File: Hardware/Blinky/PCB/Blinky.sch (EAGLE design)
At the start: 29 parts, among them Q1 IRLML2502, Q2 IRLML2502, Q3 IRLML2502, U1 ATMEGAU2-AU, U2 MTCH101, U3 TS3USB30EDGSR, X1 USB-A-PCB, X2 USB-A-PCB, Y1 ABM3

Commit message: Most of the PCB layout is done.
Still missing is the touch sensor disguised as logo (hello issue #10).
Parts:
- removed C6: 100n, rcl:C-EUC0805
- added U$1: BISS-LOGO, mibe:BISS-LOGO
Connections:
- net N$1 renamed D+_MIC
- net N$12 renamed D2-
- net N$13 renamed D2+
- net N$14 renamed D1-
- net N$15 renamed D1+
- net N$2 renamed D-_MIC
- net N$20 renamed RESET
- net N$21 renamed GND_LED_R
- net N$22 renamed GND_LED_G
- net N$23 renamed GND_LED_B
- net N$3 renamed UCAP
- net N$4 renamed TOUCH
- net N$7 renamed D+_CON
- net N$8 renamed D-_CON
- net ULEDB renamed V_LED_B
- net ULEDG renamed V_LED_G
- net ULEDR renamed V_LED_R
- new net TOUCH_PAD: U$1.P$1, U2.MTI
- net GND: now also U1.PD5; no longer C6.2
- net LED_G: now also U1.PC7
- net VCC: no longer C6.1
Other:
- moved on the sheet: C2, C3, Y1
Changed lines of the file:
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@@
 <part name="C4" library="rcl" deviceset="C-EU" device="C0805" value="100n"/>
 <part name="C5" library="rcl" deviceset="C-EU" device="C0805" value="100n"/>
-<part name="C6" library="rcl" deviceset="C-EU" device="C0805" value="100n"/>
 <part name="P+3" library="supply1" deviceset="VCC" device=""/>
 <part name="GND6" library="supply1" deviceset="GND" device=""/>
@@
 <part name="R10" library="rcl" deviceset="R-EU_" device="R0805" value="64.9"/>
 <part name="R11" library="rcl" deviceset="R-EU_" device="R0805" value="64.9"/>
+<part name="U$1" library="mibe" deviceset="BISS-LOGO" device=""/>
+<part name="GND9" library="supply1" deviceset="GND" device=""/>
 </parts>
 <sheets>
@@
 <instance part="GND2" gate="1" x="200.66" y="144.78"/>
 <instance part="GND3" gate="1" x="73.66" y="99.06"/>
-<instance part="C2" gate="G$1" x="187.96" y="114.3" rot="R90"/>
-<instance part="C3" gate="G$1" x="187.96" y="109.22" smashed="yes" rot="R90">
-<attribute name="NAME" x="187.579" y="103.124" size="1.778" layer="95" rot="R90"/>
-<attribute name="VALUE" x="192.659" y="103.124" size="1.778" layer="96" rot="R90"/>
+<instance part="C2" gate="G$1" x="193.04" y="114.3" rot="R90"/>
+<instance part="C3" gate="G$1" x="193.04" y="109.22" smashed="yes" rot="R90">
+<attribute name="NAME" x="192.659" y="103.124" size="1.778" layer="95" rot="R90"/>
+<attribute name="VALUE" x="197.739" y="103.124" size="1.778" layer="96" rot="R90"/>
 </instance>
-<instance part="GND4" gate="1" x="200.66" y="104.14"/>
-<instance part="Y1" gate="G$1" x="180.34" y="111.76" rot="R90"/>
+<instance part="GND4" gate="1" x="205.74" y="104.14"/>
+<instance part="Y1" gate="G$1" x="185.42" y="111.76" rot="R90"/>
 <instance part="R1" gate="G$1" x="121.92" y="124.46" smashed="yes">
 <attribute name="NAME" x="118.11" y="126.238" size="1.778" layer="95"/>
@@
 <instance part="C4" gate="G$1" x="63.5" y="33.02"/>
 <instance part="C5" gate="G$1" x="76.2" y="33.02"/>
-<instance part="C6" gate="G$1" x="88.9" y="33.02"/>
 <instance part="P+3" gate="VCC" x="53.34" y="40.64"/>
 <instance part="GND6" gate="1" x="53.34" y="22.86"/>
@@
 <instance part="R10" gate="G$1" x="233.68" y="93.98" rot="R90"/>
 <instance part="R11" gate="G$1" x="238.76" y="101.6" rot="R90"/>
+<instance part="U$1" gate="G$1" x="238.76" y="172.72"/>
+<instance part="GND9" gate="1" x="132.08" y="129.54"/>
 </instances>
 <busses>
@@
 <segment>
 <pinref part="GND4" gate="1" pin="GND"/>
-<wire x1="200.66" y1="114.3" x2="200.66" y2="109.22" width="0.1524" layer="91"/>
+<wire x1="205.74" y1="114.3" x2="205.74" y2="109.22" width="0.1524" layer="91"/>
 <pinref part="C2" gate="G$1" pin="2"/>
-<wire x1="200.66" y1="109.22" x2="200.66" y2="106.68" width="0.1524" layer="91"/>
-<wire x1="193.04" y1="114.3" x2="200.66" y2="114.3" width="0.1524" layer="91"/>
+<wire x1="205.74" y1="109.22" x2="205.74" y2="106.68" width="0.1524" layer="91"/>
+<wire x1="198.12" y1="114.3" x2="205.74" y2="114.3" width="0.1524" layer="91"/>
 <pinref part="C3" gate="G$1" pin="2"/>
-<wire x1="193.04" y1="109.22" x2="200.66" y2="109.22" width="0.1524" layer="91"/>
-<junction x="200.66" y="109.22"/>
+<wire x1="198.12" y1="109.22" x2="205.74" y2="109.22" width="0.1524" layer="91"/>
+<junction x="205.74" y="109.22"/>
 </segment>
 <segment>
@@
 <pinref part="GND6" gate="1" pin="GND"/>
 <wire x1="63.5" y1="25.4" x2="53.34" y2="25.4" width="0.1524" layer="91"/>
-<pinref part="C6" gate="G$1" pin="2"/>
 <wire x1="63.5" y1="25.4" x2="76.2" y2="25.4" width="0.1524" layer="91"/>
-<wire x1="76.2" y1="25.4" x2="88.9" y2="25.4" width="0.1524" layer="91"/>
-<wire x1="88.9" y1="25.4" x2="88.9" y2="27.94" width="0.1524" layer="91"/>
 <junction x="63.5" y="25.4"/>
 <pinref part="C5" gate="G$1" pin="2"/>
 <wire x1="76.2" y1="27.94" x2="76.2" y2="25.4" width="0.1524" layer="91"/>
-<junction x="76.2" y="25.4"/>
 </segment>
 <segment>
@@
 <junction x="233.68" y="45.72"/>
 </segment>
-</net>
-<net name="N$3" class="0">
+<segment>
+<pinref part="U1" gate="G$1" pin="PD5"/>
+<pinref part="GND9" gate="1" pin="GND"/>
+<wire x1="139.7" y1="134.62" x2="132.08" y2="134.62" width="0.1524" layer="91"/>
+<wire x1="132.08" y1="134.62" x2="132.08" y2="132.08" width="0.1524" layer="91"/>
+</segment>
+</net>
+<net name="UCAP" class="0">
 <segment>
 <pinref part="C1" gate="G$1" pin="1"/>
@@
 <segment>
 <pinref part="U1" gate="G$1" pin="XTAL1"/>
-<wire x1="175.26" y1="114.3" x2="180.34" y2="114.3" width="0.1524" layer="91"/>
+<wire x1="175.26" y1="114.3" x2="185.42" y2="114.3" width="0.1524" layer="91"/>
 <pinref part="Y1" gate="G$1" pin="2"/>
 <pinref part="C2" gate="G$1" pin="1"/>
-<wire x1="180.34" y1="114.3" x2="185.42" y2="114.3" width="0.1524" layer="91"/>
-<junction x="180.34" y="114.3"/>
+<wire x1="185.42" y1="114.3" x2="190.5" y2="114.3" width="0.1524" layer="91"/>
+<junction x="185.42" y="114.3"/>
 </segment>
 </net>
@@
 <pinref part="U1" gate="G$1" pin="XTAL2"/>
 <pinref part="Y1" gate="G$1" pin="1"/>
-<wire x1="180.34" y1="109.22" x2="175.26" y2="109.22" width="0.1524" layer="91"/>
+<wire x1="185.42" y1="109.22" x2="175.26" y2="109.22" width="0.1524" layer="91"/>
 <pinref part="C3" gate="G$1" pin="1"/>
-<wire x1="180.34" y1="109.22" x2="185.42" y2="109.22" width="0.1524" layer="91"/>
-<junction x="180.34" y="109.22"/>
-</segment>
-</net>
-<net name="N$1" class="0">
+<wire x1="185.42" y1="109.22" x2="190.5" y2="109.22" width="0.1524" layer="91"/>
+<junction x="185.42" y="109.22"/>
+</segment>
+</net>
+<net name="D+_MIC" class="0">
 <segment>
 <pinref part="R1" gate="G$1" pin="2"/>
@@
 </segment>
 </net>
-<net name="N$2" class="0">
+<net name="D-_MIC" class="0">
 <segment>
 <pinref part="U1" gate="G$1" pin="D-"/>
@@
 </segment>
 </net>
-<net name="N$7" class="0">
+<net name="D+_CON" class="0">
 <segment>
 <pinref part="R1" gate="G$1" pin="1"/>
@@
 </segment>
 </net>
-<net name="N$8" class="0">
+<net name="D-_CON" class="0">
 <segment>
 <pinref part="U3" gate="G$1" pin="D-"/>
@@
 <segment>
 <pinref part="U1" gate="G$1" pin="PC5"/>
-<wire x1="175.26" y1="124.46" x2="213.36" y2="124.46" width="0.1524" layer="91"/>
+<wire x1="175.26" y1="124.46" x2="180.34" y2="124.46" width="0.1524" layer="91"/>
+<wire x1="180.34" y1="124.46" x2="213.36" y2="124.46" width="0.1524" layer="91"/>
 <wire x1="213.36" y1="124.46" x2="213.36" y2="83.82" width="0.1524" layer="91"/>
 <wire x1="213.36" y1="83.82" x2="180.34" y2="83.82" width="0.1524" layer="91"/>
@@
 <wire x1="215.9" y1="43.18" x2="215.9" y2="53.34" width="0.1524" layer="91"/>
 <wire x1="215.9" y1="53.34" x2="220.98" y2="53.34" width="0.1524" layer="91"/>
+<pinref part="U1" gate="G$1" pin="PC7"/>
+<wire x1="175.26" y1="119.38" x2="180.34" y2="119.38" width="0.1524" layer="91"/>
+<wire x1="180.34" y1="119.38" x2="180.34" y2="124.46" width="0.1524" layer="91"/>
+<junction x="180.34" y="124.46"/>
 </segment>
 </net>
@@
 </segment>
 </net>
-<net name="N$12" class="0">
+<net name="D2-" class="0">
 <segment>
 <pinref part="X2" gate="G$1" pin="D-"/>
@@
 </segment>
 </net>
-<net name="N$13" class="0">
+<net name="D2+" class="0">
 <segment>
 <pinref part="U3" gate="G$1" pin="D2+"/>
@@
 </segment>
 </net>
-<net name="N$14" class="0">
+<net name="D1-" class="0">
 <segment>
 <pinref part="X1" gate="G$1" pin="D-"/>
@@
 </segment>
 </net>
-<net name="N$15" class="0">
+<net name="D1+" class="0">
 <segment>
 <pinref part="U3" gate="G$1" pin="D1+"/>
@@
 </segment>
 </net>
-<net name="N$4" class="0">
+<net name="TOUCH" class="0">
 <segment>
 <pinref part="U2" gate="G$1" pin="MTO"/>
@@
 </segment>
 </net>
-<net name="N$20" class="0">
+<net name="RESET" class="0">
 <segment>
 <pinref part="R8" gate="G$1" pin="1"/>
@@
 <segment>
 <pinref part="P+3" gate="VCC" pin="VCC"/>
-<pinref part="C6" gate="G$1" pin="1"/>
 <wire x1="53.34" y1="38.1" x2="63.5" y2="38.1" width="0.1524" layer="91"/>
 <wire x1="63.5" y1="38.1" x2="76.2" y2="38.1" width="0.1524" layer="91"/>
-<wire x1="76.2" y1="38.1" x2="88.9" y2="38.1" width="0.1524" layer="91"/>
-<wire x1="88.9" y1="38.1" x2="88.9" y2="35.56" width="0.1524" layer="91"/>
 <pinref part="C5" gate="G$1" pin="1"/>
 <wire x1="76.2" y1="35.56" x2="76.2" y2="38.1" width="0.1524" layer="91"/>
-<junction x="76.2" y="38.1"/>
 <pinref part="C4" gate="G$1" pin="1"/>
 <wire x1="63.5" y1="35.56" x2="63.5" y2="38.1" width="0.1524" layer="91"/>
@@
 </segment>
 </net>
-<net name="ULEDR" class="0">
+<net name="V_LED_R" class="0">
 <segment>
 <pinref part="R9" gate="G$1" pin="1"/>
@@
 </segment>
 </net>
-<net name="ULEDG" class="0">
+<net name="V_LED_G" class="0">
 <segment>
 <pinref part="R10" gate="G$1" pin="1"/>
@@
 </segment>
 </net>
-<net name="ULEDB" class="0">
+<net name="V_LED_B" class="0">
 <segment>
 <pinref part="R11" gate="G$1" pin="1"/>
@@
 </segment>
 </net>
-<net name="N$21" class="0">
+<net name="GND_LED_R" class="0">
 <segment>
 <pinref part="D3" gate="G$1" pin="6"/>
@@
 </segment>
 </net>
-<net name="N$22" class="0">
+<net name="GND_LED_G" class="0">
 <segment>
 <pinref part="D3" gate="G$1" pin="5"/>
@@
 </segment>
 </net>
-<net name="N$23" class="0">
+<net name="GND_LED_B" class="0">
 <segment>
 <pinref part="D3" gate="G$1" pin="4"/>
@@
 </segment>
 </net>
+<net name="TOUCH_PAD" class="0">
+<segment>
+<pinref part="U2" gate="G$1" pin="MTI"/>
+<wire x1="228.6" y1="157.48" x2="231.14" y2="157.48" width="0.1524" layer="91"/>
+<wire x1="231.14" y1="157.48" x2="231.14" y2="172.72" width="0.1524" layer="91"/>
+<pinref part="U$1" gate="G$1" pin="P$1"/>
+<wire x1="231.14" y1="172.72" x2="233.68" y2="172.72" width="0.1524" layer="91"/>
+</segment>
+</net>

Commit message: Changed the series resistance on the USB lines to 16 Ohm.
The USB switch U3 is introducing some additional resistance in the on state.
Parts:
- R1, R2: value 22 -> 16
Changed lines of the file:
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@@
 <part name="GND4" library="supply1" deviceset="GND" device=""/>
 <part name="Y1" library="mibe" deviceset="ABM3" device=""/>
-<part name="R1" library="rcl" deviceset="R-EU_" device="R0805" value="22"/>
-<part name="R2" library="rcl" deviceset="R-EU_" device="R0805" value="22"/>
+<part name="R1" library="rcl" deviceset="R-EU_" device="R0805" value="16"/>
+<part name="R2" library="rcl" deviceset="R-EU_" device="R0805" value="16"/>
 <part name="X1" library="mibe" deviceset="USB-A-PCB" device=""/>
 <part name="X2" library="mibe" deviceset="USB-A-PCB" device=""/>

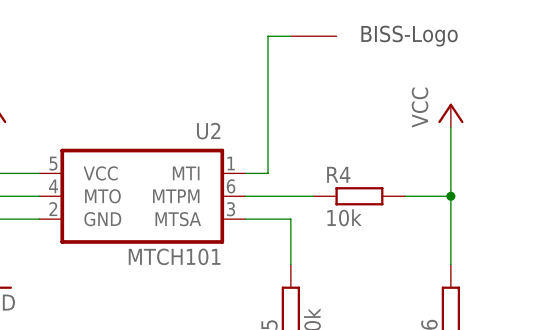
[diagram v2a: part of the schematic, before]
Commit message: Imported the BISS logo into the Blinky PCB.
This also determined the final size of the PCB.
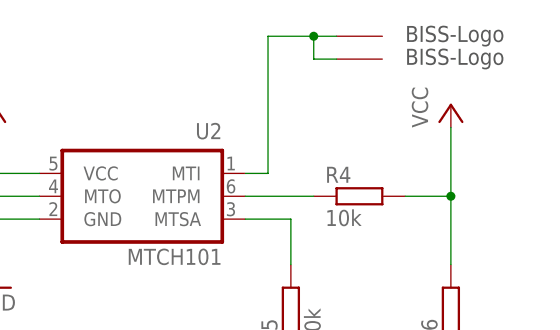
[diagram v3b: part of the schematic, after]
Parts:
- added U$2: LOGO, BISS:LOGO
- U$1: value BISS-LOGO -> LOGO; device mibe:BISS-LOGO -> BISS:LOGO
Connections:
- net TOUCH_PAD: now also U$2.P$1
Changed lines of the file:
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@@
 <part name="R10" library="rcl" deviceset="R-EU_" device="R0805" value="64.9"/>
 <part name="R11" library="rcl" deviceset="R-EU_" device="R0805" value="64.9"/>
-<part name="U$1" library="mibe" deviceset="BISS-LOGO" device=""/>
 <part name="GND9" library="supply1" deviceset="GND" device=""/>
+<part name="U$1" library="BISS" deviceset="LOGO" device=""/>
+<part name="U$2" library="BISS" deviceset="LOGO" device=""/>
 </parts>
 <sheets>
@@
 <instance part="R10" gate="G$1" x="233.68" y="93.98" rot="R90"/>
 <instance part="R11" gate="G$1" x="238.76" y="101.6" rot="R90"/>
+<instance part="GND9" gate="1" x="132.08" y="129.54"/>
 <instance part="U$1" gate="G$1" x="238.76" y="172.72"/>
-<instance part="GND9" gate="1" x="132.08" y="129.54"/>
+<instance part="U$2" gate="G$1" x="238.76" y="170.18"/>
 </instances>
 <busses>
@@
 <wire x1="231.14" y1="157.48" x2="231.14" y2="172.72" width="0.1524" layer="91"/>
 <pinref part="U$1" gate="G$1" pin="P$1"/>
-<wire x1="231.14" y1="172.72" x2="233.68" y2="172.72" width="0.1524" layer="91"/>
-</segment>
-</net>
+<wire x1="231.14" y1="172.72" x2="236.22" y2="172.72" width="0.1524" layer="91"/>
+<pinref part="U$2" gate="G$1" pin="P$1"/>
+<wire x1="236.22" y1="172.72" x2="238.76" y2="172.72" width="0.1524" layer="91"/>
+<wire x1="238.76" y1="170.18" x2="236.22" y2="170.18" width="0.1524" layer="91"/>
+<wire x1="236.22" y1="170.18" x2="236.22" y2="172.72" width="0.1524" layer="91"/>
+<junction x="236.22" y="172.72"/>
+</segment>
+</net>
